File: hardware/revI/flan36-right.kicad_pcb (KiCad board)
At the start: 2 copper layers, 113.4 x 91.3 mm, 46 parts, among them J1 BATTERY_PIGTAIL, J2 nice!view, K01 KEYSW, K02 KEYSW, K03 KEYSW, K04 KEYSW, K05 KEYSW, K11 KEYSW, K12 KEYSW, K13 KEYSW, K14 KEYSW, K15 KEYSW, K21 KEYSW, K22 KEYSW, K23 KEYSW, K24 KEYSW, K25 KEYSW, K30 KEYSW, K31 KEYSW, K32 KEYSW, SW1 SW_SPDT_PCM12, SW2 SW_SPST_TL3342, U1 nice!nano v2

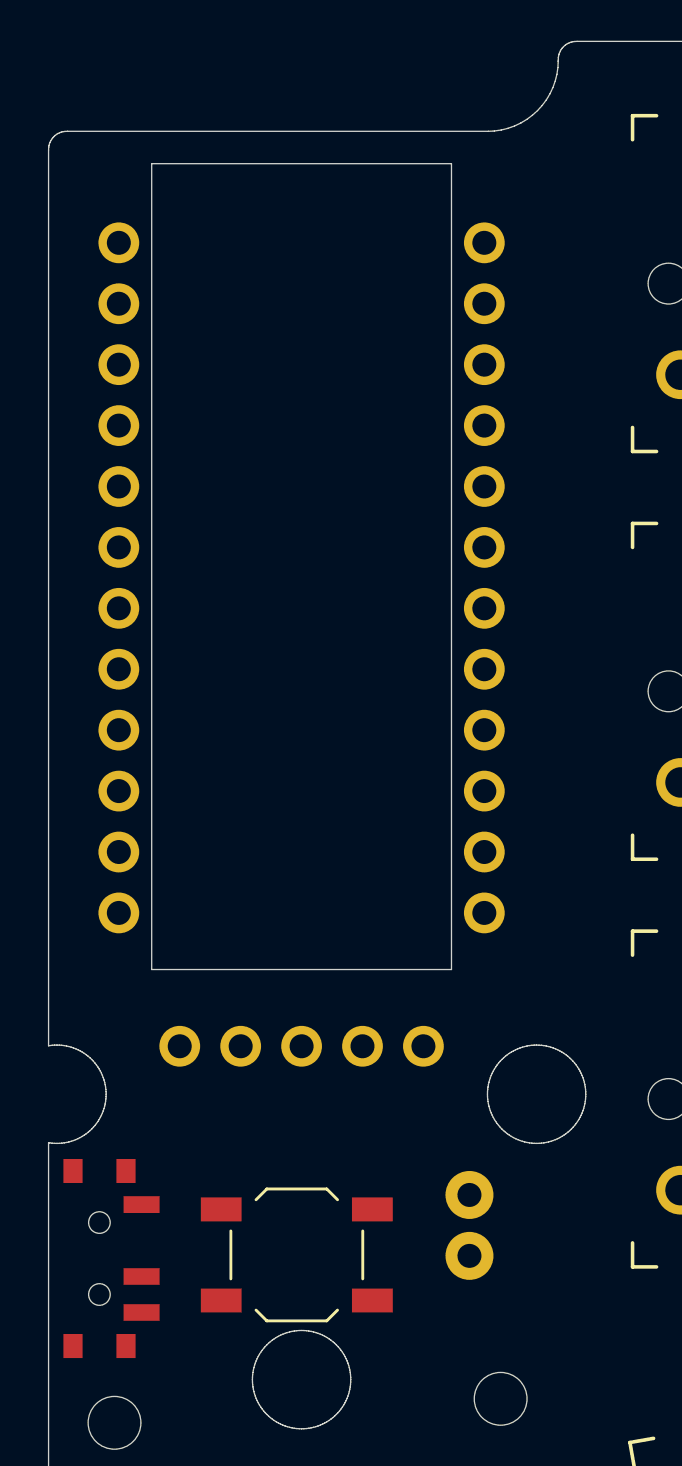
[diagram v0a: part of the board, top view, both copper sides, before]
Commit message: Lower electronics stack and add flush multicolor frame inlays
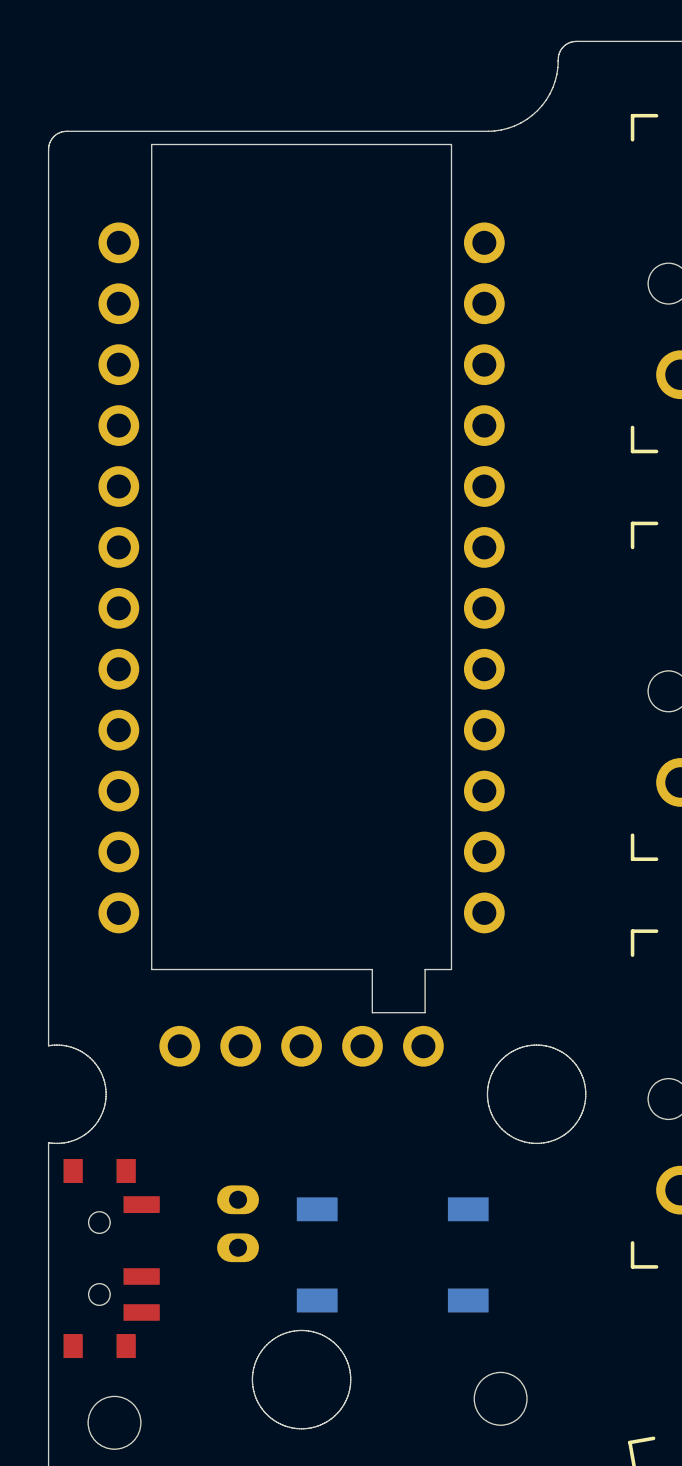
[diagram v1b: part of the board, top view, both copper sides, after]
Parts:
- J1: value BATTERY_PIGTAIL -> JST_PH_S2B-PH-K-S; footprint PiantorSlim:Battery_pigtail_2.54 -> PiantorSlim:JST_PH_S2B-PH-K_1x02_P2.00mm_Horizontal
- SW2: moved to B.Cu
- moved J1 9.90 mm to (34.5, 59.2), turned to 90 degrees
- moved SW2 4.00 mm to (41.0, 59.5)
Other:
- outline, holes or cut-outs redrawn

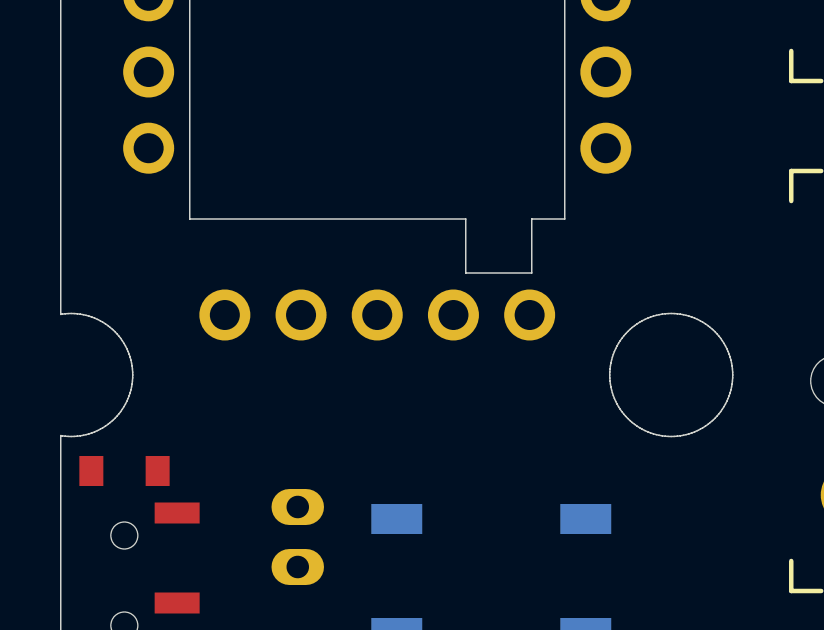
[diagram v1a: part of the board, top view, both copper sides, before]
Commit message: Implement five approved R4 frames with exact CAD and print geometry
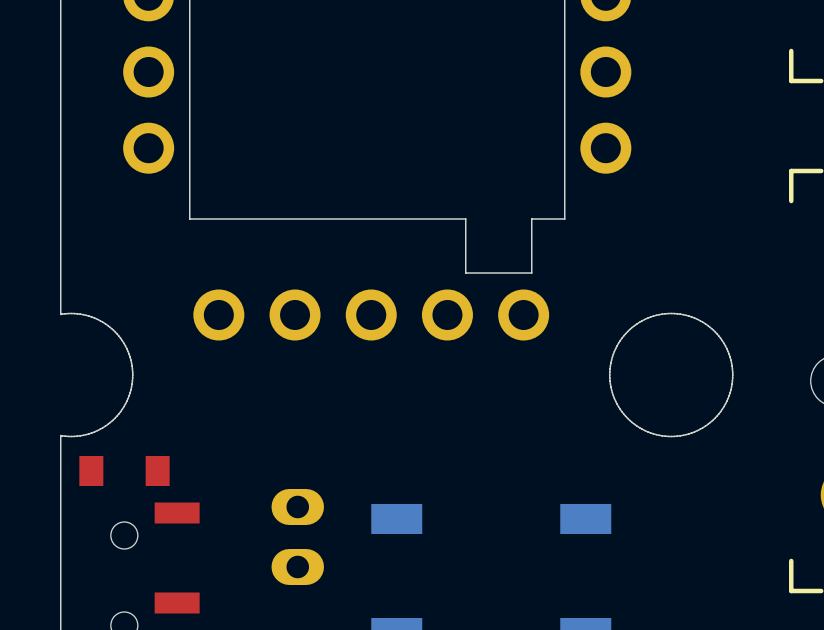
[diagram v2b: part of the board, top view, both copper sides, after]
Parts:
- moved J2 0.20 mm to (31.9, 50.8)
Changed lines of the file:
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@@
 	(footprint "PiantorSlim:nice_view_5pin"
 		(layer "F.Cu")
-		(at 32.12 50.8)
+		(at 31.920000 50.8)
 		(property "Reference" "J2"
 			(at 0 0 0)
